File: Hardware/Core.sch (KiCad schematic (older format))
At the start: 23 parts

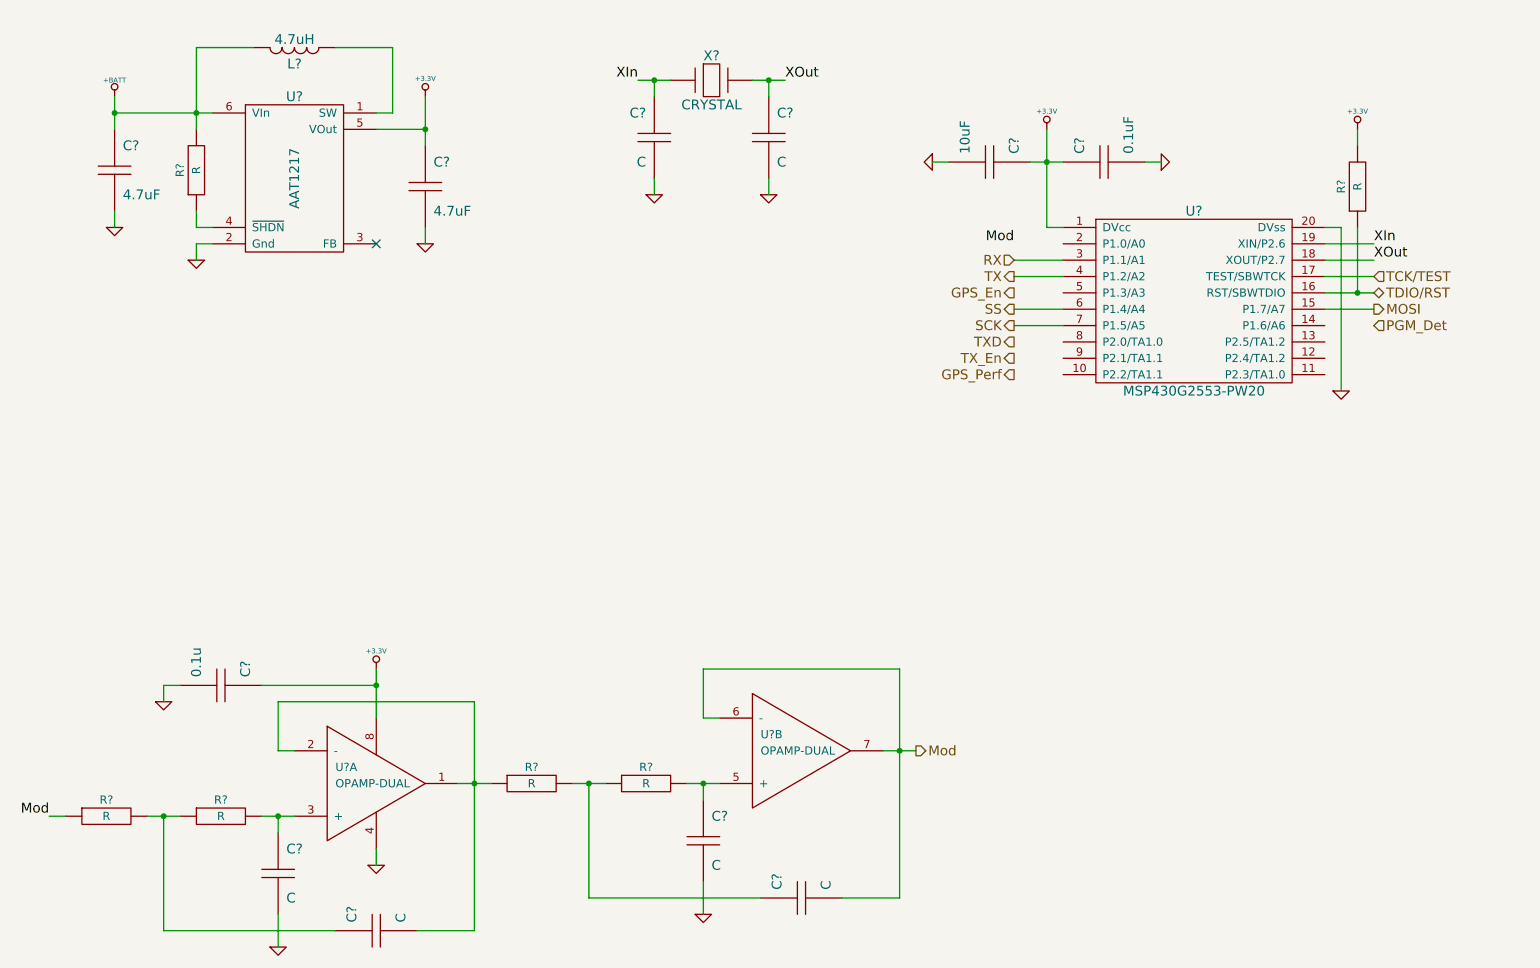
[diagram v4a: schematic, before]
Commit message: Voltage regulator values
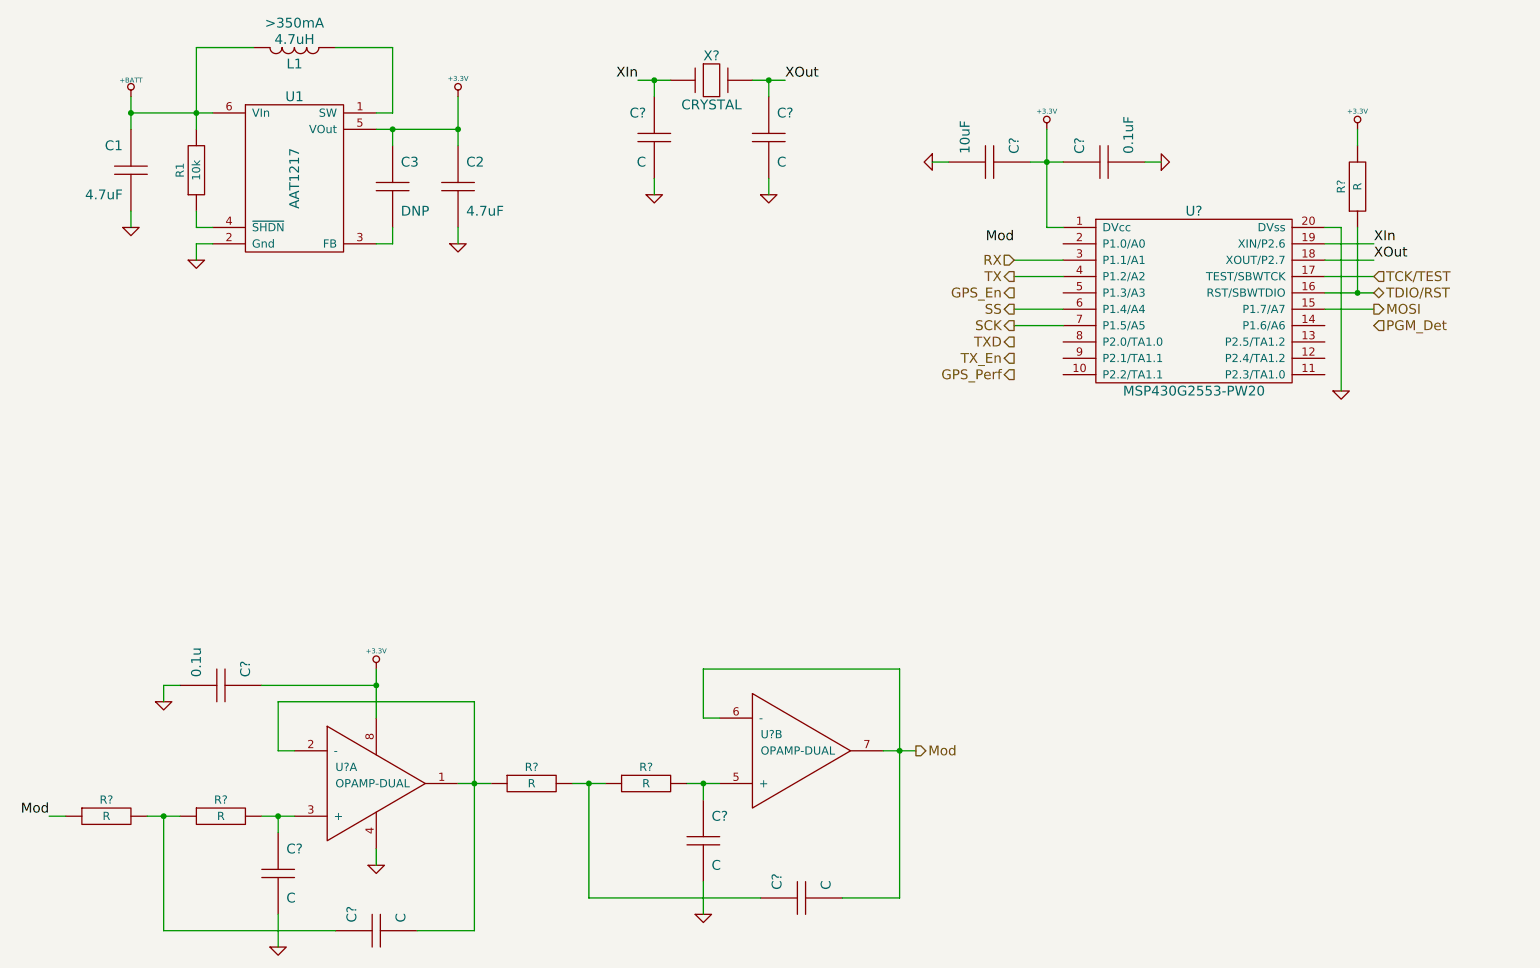
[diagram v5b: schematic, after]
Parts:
- removed C?: 4.7uF, ~, symbol C
- added C2: 4.7uF, CAPC2012-N, symbol C
- added C3: DNP, CAPC1608-N, symbol C
- C1: renamed from C?; footprint ~ -> CAPC2012-N; Dielectric D -> X5R; Distributor Part No (none) -> 1276-1065-1-ND; MFR Name (none) -> Samsung; MFR Part No (none) -> CL21A475KOFNNNE; Voltage V -> 16V
- L1: renamed from L?; footprint ~ -> INDC3225-N; Current (none) -> >350mA; Distributor Part No (none) -> 587-2166-1-ND; MFR Name (none) -> Taiyo Yuden; MFR Part No (none) -> BRL3225T4R7M
- R1: renamed from R?; value R -> 10k; footprint ~ -> RESC1608-N; Distributor Part No (none) -> 311-10KGRCT-ND; MFR Name (none) -> Yageo; MFR Part No (none) -> RC0603JR-0710KL; Power W -> 0.1W; Tolerance % -> 5%
- U1: renamed from U?; Distributor Part No (none) -> 863-1496-1-ND; MFR Name (none) -> Skyworks; MFR Part No (none) -> AAT1217ICA-3.3-T1
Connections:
- net +3.3V: now also C2.1, C3.1
- net GND: now also C2.2
- net at U1.3 (FB): now also C3.2
- no-connect marks 1 -> 0
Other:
- moved on the sheet: C1
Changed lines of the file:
@@
 $EndDescr
 $Comp
-L AAT1217 U?
+L AAT1217 U1
 U 1 1 52ECD611
 P 2600 2300
-F 0 "U?" H 2600 2800 60  0000 C CNN
+F 0 "U1" H 2600 2800 60  0000 C CNN
 F 1 "AAT1217" V 2600 2300 60  0000 C CNN
 F 2 "" H 2600 2300 60  0000 C CNN
 F 3 "" H 2600 2300 60  0000 C CNN
+F 4 "Skyworks" H 2600 2300 60  0001 C CNN "MFR Name"
+F 5 "AAT1217ICA-3.3-T1" H 2600 2300 60  0001 C CNN "MFR Part No"
+F 6 "863-1496-1-ND" H 2600 2300 60  0001 C CNN "Distributor Part No"
 	1    2600 2300
 	1    0    0    -1
 $EndComp
 $Comp
-L L L?
+L L L1
 U 1 1 52ECD617
 P 2600 1500
-F 0 "L?" H 2600 1400 60  0000 C CNN
+F 0 "L1" H 2600 1400 60  0000 C CNN
 F 1 "4.7uH" H 2600 1550 60  0000 C CNN
-F 2 "~" H 2600 1500 60  0000 C CNN
+F 2 "INDC3225-N" H 2600 1500 60  0001 C CNN
 F 3 "~" H 2600 1500 60  0000 C CNN
+F 4 "Taiyo Yuden" H 2600 1500 60  0001 C CNN "MFR Name"
+F 5 "BRL3225T4R7M" H 2600 1500 60  0001 C CNN "MFR Part No"
+F 6 "587-2166-1-ND" H 2600 1500 60  0001 C CNN "Distributor Part No"
+F 7 ">350mA" H 2600 1650 60  0000 C CNN "Current"
 	1    2600 1500
 	1    0    0    -1
 $EndComp
 $Comp
-L C C?
-U 1 1 52ECD61F
-P 3400 2350
-F 0 "C?" H 3450 2500 60  0000 L CNN
-F 1 "4.7uF" H 3450 2200 60  0000 L CNN
-F 2 "~" H 3400 2350 60  0000 C CNN
-F 3 "~" H 3400 2350 60  0000 C CNN
-F 4 "V" H 3350 2200 60  0001 R CNN "Voltage"
-F 5 "D" H 3350 2500 60  0001 R CNN "Dielectric"
-	1    3400 2350
-	1    0    0    -1
-$EndComp
-NoConn ~ 3100 2700
-$Comp
-L R R?
+L R R1
 U 1 1 52ECD628
 P 2000 2250
-F 0 "R?" H 2000 2350 50  0000 C CNN
-F 1 "R" H 2000 2250 50  0000 C CNN
-F 2 "~" H 2000 2250 60  0000 C CNN
+F 0 "R1" H 2000 2350 50  0000 C CNN
+F 1 "10k" H 2000 2250 50  0000 C CNN
+F 2 "RESC1608-N" H 2000 2250 60  0001 C CNN
 F 3 "~" H 2000 2250 60  0000 C CNN
-F 4 "W" H 2000 2150 50  0001 C CNN "Power"
-F 5 "%" H 2000 2050 50  0001 C CNN "Tolerance"
+F 4 "Yageo" H 2000 2250 60  0001 C CNN "MFR Name"
+F 5 "RC0603JR-0710KL" H 2000 2250 60  0001 C CNN "MFR Part No"
+F 6 "311-10KGRCT-ND" H 2000 2250 60  0001 C CNN "Distributor Part No"
+F 7 "0.1W" H 2000 2150 50  0001 C CNN "Power"
+F 8 "5%" H 2000 2050 50  0001 C CNN "Tolerance"
 	1    2000 2250
 	0    -1   -1   0
 $EndComp
 $Comp
-L C C?
+L C C1
 U 1 1 52ECD632
-P 1500 2250
-F 0 "C?" H 1550 2400 60  0000 L CNN
-F 1 "4.7uF" H 1550 2100 60  0000 L CNN
-F 2 "~" H 1500 2250 60  0000 C CNN
-F 3 "~" H 1500 2250 60  0000 C CNN
-F 4 "V" H 1450 2100 60  0001 R CNN "Voltage"
-F 5 "D" H 1450 2400 60  0001 R CNN "Dielectric"
-	1    1500 2250
-	1    0    0    -1
+P 1600 2250
+F 0 "C1" H 1650 2400 60  0000 L CNN
+F 1 "4.7uF" H 1650 2100 60  0000 L CNN
+F 2 "CAPC2012-N" H 1600 2250 60  0001 C CNN
+F 3 "~" H 1600 2250 60  0000 C CNN
+F 4 "Samsung" H 1600 2250 60  0001 C CNN "MFR Name"
+F 5 "CL21A475KOFNNNE" H 1600 2250 60  0001 C CNN "MFR Part No"
+F 6 "1276-1065-1-ND" H 1600 2250 60  0001 C CNN "Distributor Part No"
+F 7 "16V" H 1550 2100 60  0001 R CNN "Voltage"
+F 8 "X5R" H 1550 2400 60  0001 R CNN "Dielectric"
+	1    1600 2250
+	-1   0    0    -1
 $EndComp
 $Comp
 L +BATT #PWR?
 U 1 1 52ECD638
-P 1500 1800
-F 0 "#PWR?" H 1500 1750 20  0001 C CNN
-F 1 "+BATT" H 1500 1900 30  0000 C CNN
-F 2 "" H 1500 1800 60  0000 C CNN
-F 3 "" H 1500 1800 60  0000 C CNN
-	1    1500 1800
+P 1600 1800
+F 0 "#PWR?" H 1600 1750 20  0001 C CNN
+F 1 "+BATT" H 1600 1900 30  0000 C CNN
+F 2 "" H 1600 1800 60  0000 C CNN
+F 3 "" H 1600 1800 60  0000 C CNN
+	1    1600 1800
 	1    0    0    -1
 $EndComp
@@
 L GND #PWR?
 U 1 1 52ECD64A
-P 3400 2700
-F 0 "#PWR?" H 3400 2700 30  0001 C CNN
-F 1 "GND" H 3400 2630 30  0001 C CNN
-F 2 "" H 3400 2700 60  0000 C CNN
-F 3 "" H 3400 2700 60  0000 C CNN
-	1    3400 2700
+P 3600 2700
+F 0 "#PWR?" H 3600 2700 30  0001 C CNN
+F 1 "GND" H 3600 2630 30  0001 C CNN
+F 2 "" H 3600 2700 60  0000 C CNN
+F 3 "" H 3600 2700 60  0000 C CNN
+	1    3600 2700
 	1    0    0    -1
 $EndComp
@@
 L GND #PWR?
 U 1 1 52ECD650
-P 1500 2600
-F 0 "#PWR?" H 1500 2600 30  0001 C CNN
-F 1 "GND" H 1500 2530 30  0001 C CNN
-F 2 "" H 1500 2600 60  0000 C CNN
-F 3 "" H 1500 2600 60  0000 C CNN
-	1    1500 2600
+P 1600 2600
+F 0 "#PWR?" H 1600 2600 30  0001 C CNN
+F 1 "GND" H 1600 2530 30  0001 C CNN
+F 2 "" H 1600 2600 60  0000 C CNN
+F 3 "" H 1600 2600 60  0000 C CNN
+	1    1600 2600
 	1    0    0    -1
 $EndComp
@@
 L +3.3V #PWR?
 U 1 1 52ECD663
-P 3400 1800
-F 0 "#PWR?" H 3400 1760 30  0001 C CNN
-F 1 "+3.3V" H 3400 1910 30  0000 C CNN
-F 2 "" H 3400 1800 60  0000 C CNN
-F 3 "" H 3400 1800 60  0000 C CNN
-	1    3400 1800
+P 3600 1800
+F 0 "#PWR?" H 3600 1760 30  0001 C CNN
+F 1 "+3.3V" H 3600 1910 30  0000 C CNN
+F 2 "" H 3600 1800 60  0000 C CNN
+F 3 "" H 3600 1800 60  0000 C CNN
+	1    3600 1800
 	1    0    0    -1
 $EndComp
@@
 	2000 2600 2100 2600
 Wire Wire Line
-	1500 1800 1500 2000
-Wire Wire Line
-	1500 1900 2100 1900
-Connection ~ 1500 1900
-Wire Wire Line
-	2000 1500 2000 2000
+	1600 1800 1600 1900
+Wire Wire Line
+	1600 1900 1600 2000
+Wire Wire Line
+	1600 1900 2000 1900
+Wire Wire Line
+	2000 1900 2100 1900
+Connection ~ 1600 1900
+Wire Wire Line
+	2000 1500 2000 1900
+Wire Wire Line
+	2000 1900 2000 2000
 Connection ~ 2000 1900
 Wire Wire Line
 	2000 1500 2350 1500
 Wire Wire Line
-	3100 2000 3400 2000
-Wire Wire Line
-	3400 1800 3400 2100
+	3100 2000 3200 2000
+Wire Wire Line
+	3200 2000 3600 2000
+Wire Wire Line
+	3600 1800 3600 2000
+Wire Wire Line
+	3600 2000 3600 2100
 Wire Wire Line
 	2000 2800 2000 2700
@@
 	2000 2700 2100 2700
 Wire Wire Line
-	1500 2500 1500 2600
-Wire Wire Line
-	3400 2600 3400 2700
+	1600 2500 1600 2600
+Wire Wire Line
+	3600 2600 3600 2700
 Wire Wire Line
 	2850 1500 3200 1500
@@
 Wire Wire Line
 	3200 1900 3100 1900
-Connection ~ 3400 2000
+Connection ~ 3600 2000
 Wire Wire Line
 	9000 3600 9000 2600
@@
 	8900 2900 9200 2900
 Wire Wire Line
-	8900 3000 9200 3000
+	8900 3000 9100 3000
+Wire Wire Line
+	9100 3000 9200 3000
 Wire Wire Line
 	9100 2600 9100 3000
@@
 	9100 2000 9100 2100
 Wire Wire Line
-	7200 2000 7200 2600
+	7200 2000 7200 2200
+Wire Wire Line
+	7200 2200 7200 2600
 Wire Wire Line
 	7200 2600 7300 2600
@@
 	6500 2200 6600 2200
 Wire Wire Line
-	7100 2200 7300 2200
+	7100 2200 7200 2200
+Wire Wire Line
+	7200 2200 7300 2200
 Connection ~ 7200 2200
 Wire Wire Line
@@
 	2500 6800 2500 7000
 Wire Wire Line
-	1700 6200 1900 6200
+	1700 6200 1800 6200
+Wire Wire Line
+	1800 6200 1900 6200
 Wire Wire Line
 	1800 6200 1800 6900
 Wire Wire Line
-	3700 5500 3700 6900
-Wire Wire Line
-	3600 6000 3800 6000
+	3700 5500 3700 6000
+Wire Wire Line
+	3700 6000 3700 6900
+Wire Wire Line
+	3600 6000 3700 6000
+Wire Wire Line
+	3700 6000 3800 6000
 Connection ~ 1800 6200
 Wire Wire Line
@@
 	3100 6400 3100 6500
 Wire Wire Line
-	2400 6200 2600 6200
+	2400 6200 2500 6200
+Wire Wire Line
+	2500 6200 2600 6200
 Wire Wire Line
 	2500 6300 2500 6200
@@
 	3700 6900 3350 6900
 Wire Wire Line
-	4300 6000 4500 6000
-Wire Wire Line
-	5000 6000 5200 6000
+	4300 6000 4400 6000
+Wire Wire Line
+	4400 6000 4500 6000
+Wire Wire Line
+	5000 6000 5100 6000
+Wire Wire Line
+	5100 6000 5200 6000
 Wire Wire Line
 	5100 6100 5100 6000
@@
 	5100 5300 6300 5300
 Wire Wire Line
-	6300 5300 6300 6700
-Wire Wire Line
-	6200 5800 6400 5800
+	6300 5300 6300 5800
+Wire Wire Line
+	6300 5800 6300 6700
+Wire Wire Line
+	6200 5800 6300 5800
+Wire Wire Line
+	6300 5800 6400 5800
 Wire Wire Line
 	6300 6700 5950 6700
@@
 $EndComp
 Wire Wire Line
-	3100 5300 3100 5600
+	3100 5300 3100 5400
+Wire Wire Line
+	3100 5400 3100 5600
 Wire Wire Line
 	2400 5400 3100 5400
@@
 XIn
 Wire Wire Line
-	4700 1700 4900 1700
-Wire Wire Line
-	5400 1700 5600 1700
+	4700 1700 4800 1700
+Wire Wire Line
+	4800 1700 4900 1700
+Wire Wire Line
+	5400 1700 5500 1700
+Wire Wire Line
+	5500 1700 5600 1700
 Wire Wire Line
 	5500 1800 5500 1700
@@
 Wire Wire Line
 	8900 2800 9200 2800
+$Comp
+L C C3
+U 1 1 52EF39D3
+P 3200 2350
+F 0 "C3" H 3250 2500 60  0000 L CNN
+F 1 "DNP" H 3250 2200 60  0000 L CNN
+F 2 "CAPC1608-N" H 3200 2350 60  0001 C CNN
+F 3 "~" H 3200 2350 60  0000 C CNN
+F 4 "V" H 3150 2200 60  0001 R CNN "Voltage"
+F 5 "D" H 3150 2500 60  0001 R CNN "Dielectric"
+	1    3200 2350
+	1    0    0    -1
+$EndComp
+Wire Wire Line
+	3200 2100 3200 2000
+Connection ~ 3200 2000
+Wire Wire Line
+	3200 2600 3200 2700
+Wire Wire Line
+	3200 2700 3100 2700
+$Comp
+L C C2
+U 1 1 52EF6065
+P 3600 2350
+F 0 "C2" H 3650 2500 60  0000 L CNN
+F 1 "4.7uF" H 3650 2200 60  0000 L CNN
+F 2 "CAPC2012-N" H 3600 2350 60  0001 C CNN
+F 3 "~" H 3600 2350 60  0000 C CNN
+F 4 "Samsung" H 3600 2350 60  0001 C CNN "MFR Name"
+F 5 "CL21A475KOFNNNE" H 3600 2350 60  0001 C CNN "MFR Part No"
+F 6 "1276-1065-1-ND" H 3600 2350 60  0001 C CNN "Distributor Part No"
+F 7 "16V" H 3550 2200 60  0001 R CNN "Voltage"
+F 8 "X5R" H 3550 2500 60  0001 R CNN "Dielectric"
+	1    3600 2350
+	1    0    0    -1
+$EndComp
 $EndSCHEMATC
